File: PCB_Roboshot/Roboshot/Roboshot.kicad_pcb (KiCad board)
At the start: 2 copper layers, 78.3 x 91.9 mm, 28 parts, among them J1 Conn_01x01, J2 Conn_01x08, J3 Conn_01x04, J5 Conn_01x01, Q1_LIGHT1 BC546, Q2_PUMP_DC1 BC546, U1 7840-0000PR

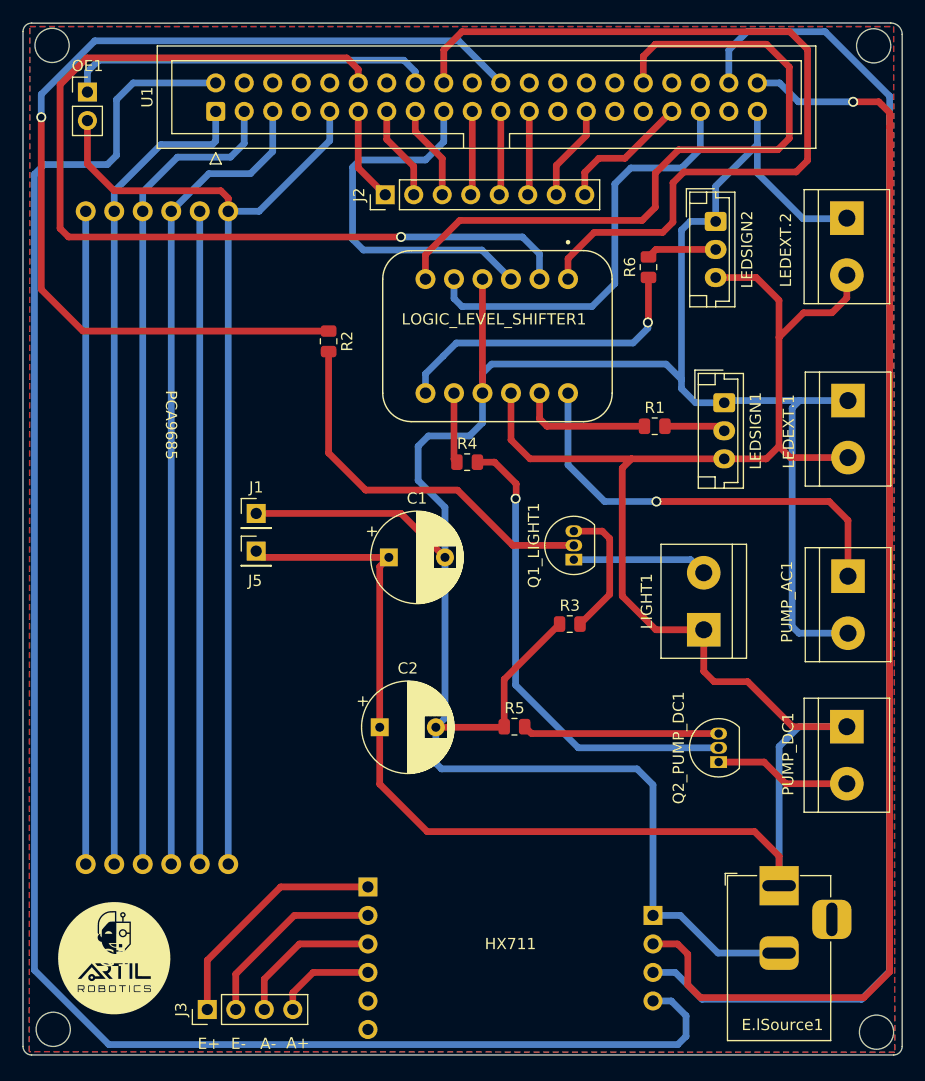
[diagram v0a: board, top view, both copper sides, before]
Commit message: Cambios en PCB roboshot_final
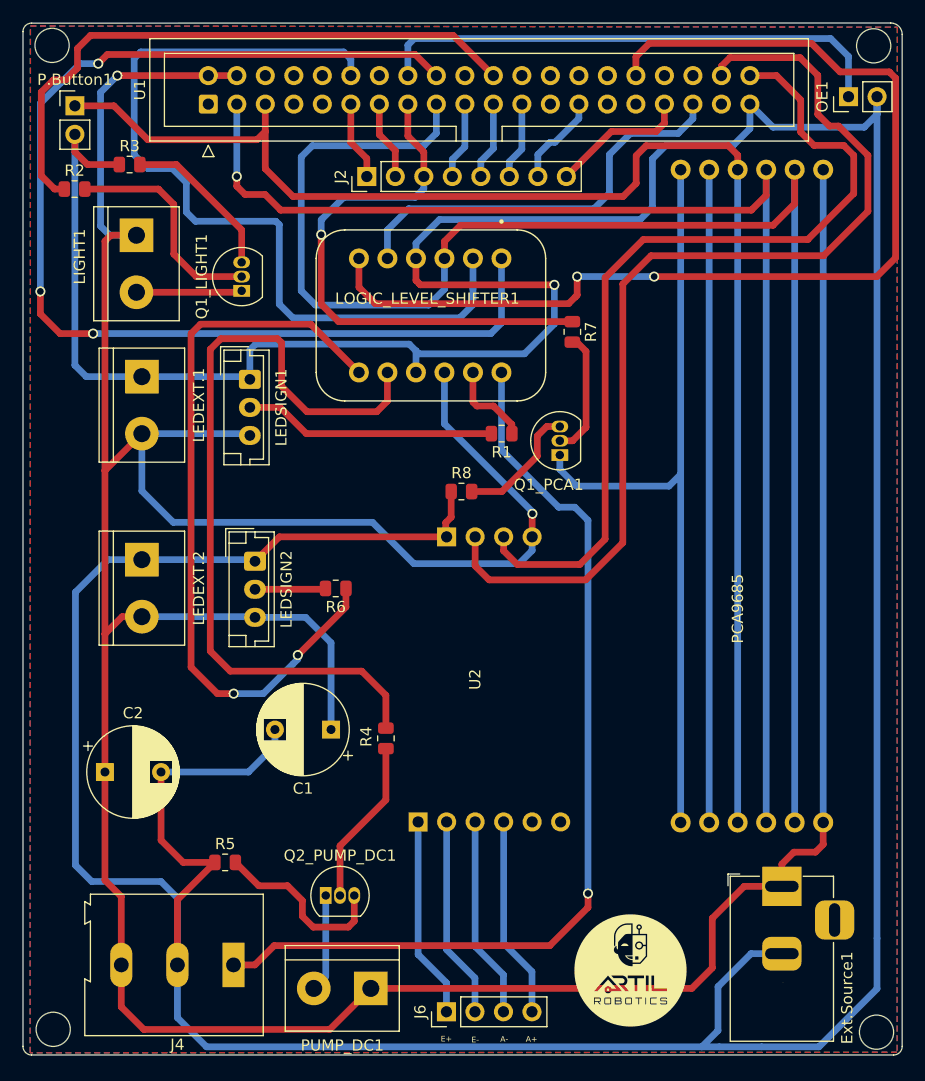
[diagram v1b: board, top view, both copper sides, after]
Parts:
- removed E.lSource1: Conn_01x02, Connector_BarrelJack:BarrelJack_Horizontal
- removed G1: LOGO, Sellos:Sello_completo
- removed HX711: DualChannel, DualChannel_HX711:Dual Channel
- removed J1, J5: Conn_01x01, Connector_PinHeader_2.54mm:PinHeader_1x01_P2.54mm_Vertical
- removed J3: Conn_01x04, Connector_PinHeader_2.54mm:PinHeader_1x04_P2.54mm_Vertical
- removed PUMP_AC1: Conn_01x02, TerminalBlock:TerminalBlock_bornier-2_P5.08mm
- added Ext.Source1: Conn_01x02, Connector_BarrelJack:BarrelJack_Horizontal, F.Cu at (291.9, 185.3)
- added G: LOGO, Sensor:Sello1_artil, F.Cu at (278.4, 192.8)
- added J4: Conn_01x03, TerminalBlock:TerminalBlock_Altech_AK300-3_P5.00mm, F.Cu at (243.0, 192.3)
- added J6: Conn_01x04, Connector_PinHeader_2.54mm:PinHeader_1x04_P2.54mm_Vertical, F.Cu at (262.0, 196.4)
- added P.Button1: Conn_01x02, Connector_PinHeader_2.54mm:PinHeader_1x02_P2.54mm_Vertical, F.Cu at (228.9, 115.7)
- added Q1_PCA1: BC546, Package_TO_SOT_THT:TO-92_Inline, F.Cu at (272.1, 146.8)
- added R7: R, Resistor_SMD:R_0805_2012Metric, F.Cu at (273.2, 135.9)
- added R8: R, Resistor_SMD:R_0805_2012Metric, F.Cu at (263.3, 150.1)
- added U2: H, DualChannel_HX711:Dual Channel, F.Cu at (272.2, 179.5)
- moved LEDEXT.2 69.8 mm to (234.9, 156.2)
- moved OE1 67.8 mm to (297.8, 114.9), turned to 90 degrees
- moved LEDEXT.1 63.0 mm to (234.9, 139.9)
- moved LIGHT1 61.6 mm to (234.4, 127.3), turned to -90 degrees
- moved R3 56.7 mm to (233.8, 121.0)
- moved PCA9685 54.0 mm to (288.5, 160.5), turned to 90 degrees
- moved LEDSIGN2 51.0 mm to (245.0, 156.3)
- moved PUMP_DC1 48.4 mm to (255.3, 194.4), turned to 180 degrees
- moved LEDSIGN1 42.3 mm to (244.5, 140.1)
- moved R6 39.9 mm to (252.1, 158.7), turned to 180 degrees
- moved Q1_LIGHT1 38.1 mm to (243.8, 132.2)
- moved Q2_PUMP_DC1 37.0 mm to (251.3, 186.1), turned to 0 degrees
- moved R5 28.5 mm to (242.3, 183.1)
- moved R2 26.4 mm to (228.9, 123.1), turned to 0 degrees
- moved R4 25.7 mm to (256.6, 172.1), turned to -90 degrees
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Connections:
- C1 pad 1: +5VA -> +5V
- C2 pad 1: +5VA -> +5V
- LEDEXT.1 pad 2: +5VA -> +5V
- LEDEXT.2 pad 2: +5VA -> +5V
- LEDSIGN1 pad 3: +5VA -> +5V
- LEDSIGN2 pad 3: +5VA -> +5V
- LIGHT1 pad 1: +5VA -> +5V
- LOGIC_LEVEL_SHIFTER1 pad HV: +5VA -> +5V
- PCA9685 pad GND_1: GND -> /GND_PCA9685
- PCA9685 pad GND_2: GND -> /GND_PCA9685
- PCA9685 pad V+_1: Net-(PCA9685-PadV+_1) -> +5V
- PCA9685 pad V+_2: Net-(PCA9685-PadV+_1) -> +5V
- PUMP_DC1 pad 1: +5VA -> +5V
- U1 pad 1: +3V3 -> unconnected-(U1-Pad1)
- U1 pad 14: GND -> unconnected-(U1-Pad14)
- U1 pad 20: GND -> unconnected-(U1-Pad20)
- U1 pad 25: GND -> unconnected-(U1-Pad25)
- U1 pad 30: GND -> unconnected-(U1-Pad30)
- U1 pad 34: GND -> unconnected-(U1-Pad34)
- U1 pad 6: GND -> unconnected-(U1-Pad6)
- U1 pad 9: GND -> unconnected-(U1-Pad9)
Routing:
- net +5VA: track 197.0 -> 0.00 mm
- net +5V: track 159.8 -> 340.0 mm, vias 0 -> 2
- net GND: track 322.9 -> 425.7 mm, vias 0 -> 1
- net /GND_PCA9685: track 0.00 -> 71.3 mm
- net /HV3: track 6.26 -> 71.2 mm
- net Net-(PCA9685-PadV+_1): track 58.2 -> 0.00 mm
- net /GPIO3(SCL1): track 73.0 -> 130.5 mm
- net /HV1: track 38.4 -> 85.4 mm
- net /GPIO2(SDA1): track 73.6 -> 116.3 mm, vias 0 -> 1
- net /GPIO22(GEN3): track 8.42 -> 49.0 mm, vias 0 -> 1
- net /HV4: track 27.8 -> 66.6 mm, vias 1 -> 2
- net /GPIO21(SPI1_SCK): track 115.1 -> 77.5 mm, vias 1 -> 0
- net /GPIO25(GEN6): track 89.0 -> 54.9 mm, vias 1 -> 0
- net /GPIO12(PWM0): track 63.7 -> 96.2 mm, vias 0 -> 2
- net +3V3: track 107.3 -> 139.4 mm
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
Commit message: Placa final_Roboshot
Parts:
- removed G: LOGO, Sensor:Sello1_artil
- removed J4: Conn_01x03, TerminalBlock:TerminalBlock_Altech_AK300-3_P5.00mm
- removed P.Button1: Conn_01x02, Connector_PinHeader_2.54mm:PinHeader_1x02_P2.54mm_Vertical
- removed Q1_PCA1, Q2_PUMP_DC1: BC546, Package_TO_SOT_THT:TO-92_Inline
- removed R3: R, Resistor_SMD:R_0805_2012Metric
- removed U2: H, DualChannel_HX711:Dual Channel
- added B.OUTPUT1: BC546, Package_TO_SOT_THT:TO-92_Inline, F.Cu at (239.2, 128.0)
- added BUTTON1: BC546, Package_TO_SOT_THT:TO-92_Inline, F.Cu at (248.7, 183.0)
- added D1: LED, LED_THT:LED_D3.0mm, F.Cu at (228.5, 120.3)
- added HX711: H, DualChannel_HX711:Dual Channel, F.Cu at (268.5, 191.6)
- added IRFZ44N: BSP89, Package_TO_SOT_THT:SIPAK_Vertical, F.Cu at (243.3, 169.1)
- added Q_PCA9685: BC546, Package_TO_SOT_THT:TO-92_Inline, F.Cu at (272.8, 132.9)
- added R10: R, Resistor_SMD:R_0805_2012Metric, F.Cu at (251.8, 188.9)
- added R9: R, Resistor_SMD:R_0805_2012Metric, F.Cu at (231.3, 114.6)
- added ROBOSHOT: ROBOSHOT, Symbol:Sello-ArtilRobotics, F.Cu at (277.8, 193.3)
- added SOLID RELE: Conn_01x03, TerminalBlock:TerminalBlock_Altech_AK300-3_P5.00mm, F.Cu at (234.4, 193.0)
- added SW1: SW_Push_Dual_x2, Connector_PinHeader_2.54mm:PinHeader_1x02_P2.54mm_Vertical, F.Cu at (232.3, 125.9)
- moved R2 71.2 mm to (299.9, 118.1), turned to -90 degrees
- moved OE1 68.0 mm to (231.9, 131.7)
- moved R8 54.5 mm to (227.0, 190.7), turned to -90 degrees
- moved LIGHT1 50.2 mm to (230.7, 177.3)
- moved Q1_LIGHT1 45.5 mm to (242.7, 177.7)
- moved PUMP_DC1 37.7 mm to (230.7, 165.8), turned to -90 degrees
- moved R5 36.0 mm to (238.5, 147.4), turned to 90 degrees
- moved C2 31.8 mm to (256.0, 154.7)
- moved R7 28.8 mm to (299.6, 124.3)
- moved C1 27.1 mm to (271.7, 153.0)
- moved LEDSIGN2 19.6 mm to (243.3, 136.7)
- moved LEDEXT.2 19.1 mm to (230.9, 137.4)
- moved R6 14.7 mm to (252.1, 144.0)
- moved LEDEXT.1 12.8 mm to (230.9, 152.0)
- moved LEDSIGN1 12.3 mm to (243.5, 152.3)
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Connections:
- LIGHT1 pad 1: +5V -> /LIGHT
- LIGHT1 pad 2: /LIGHT -> GND
- LOGIC_LEVEL_SHIFTER1 pad LV1: /GPIO24(GEN5) -> /GPIO12(PWM0)
- LOGIC_LEVEL_SHIFTER1 pad LV2: /GPIO18(GEN1)(PWM0) -> /GPIO19(SPI1_MISO)
- LOGIC_LEVEL_SHIFTER1 pad LV3: /GPIO19(SPI1_MISO) -> /GPIO18(GEN1)(PWM0)
- LOGIC_LEVEL_SHIFTER1 pad LV4: /GPIO12(PWM0) -> /GPIO24(GEN5)
- PCA9685 pad GND_1: /GND_PCA9685 -> GND
- PCA9685 pad GND_2: /GND_PCA9685 -> GND
- PCA9685 pad V+_1: +5V -> /2N_PCA9685
- PCA9685 pad V+_2: +5V -> /2N_PCA9685
- PCA9685 pad VCC_1: +3V3 -> +5V
- PCA9685 pad VCC_2: +3V3 -> +5V
- Q1_LIGHT1 pad 1: /LIGHT -> +5V
- Q1_LIGHT1 pad 3: Net-(Q1_LIGHT1-Pad3) -> /LIGHT
- R1 pad 1: /HV2 -> /HV1
- R4 pad 1: /HV3 -> /HV2
- R4 pad 2: Net-(Q2_PUMP_DC1-Pad2) -> GND
- R5 pad 1: GND -> +5V
- R6 pad 1: /HV4 -> /HV3
- R7 pad 1: /GPIO22(GEN3) -> /GPIO26
- R8 pad 1: GND -> /GPIO14(TXD0)
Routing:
- net +3V3: track 139.4 -> 26.0 mm
- net /GPIO14(TXD0): track 0.00 -> 99.9 mm
- net Net-(Q1_LIGHT1-Pad2): track 19.8 -> 116.4 mm
- net /2N_PCA9685: track 0.00 -> 87.7 mm
- net /HV1: track 85.4 -> 3.57 mm, vias 1 -> 0
- net /GPIO20(SPI1_MOSI): track 90.1 -> 164.7 mm, vias 0 -> 1
- net /GPIO21(SPI1_SCK): track 77.5 -> 149.0 mm, vias 0 -> 1
- net /GND_PCA9685: track 71.3 -> 0.00 mm
- net /HV3: track 71.2 -> 5.01 mm
- net /GPIO24(GEN5): track 104.6 -> 56.8 mm, vias 3 -> 0
- net /HV2: track 7.75 -> 51.3 mm, vias 0 -> 1
- net /GPIO22(GEN3): track 49.0 -> 7.44 mm, vias 1 -> 0
- net /GPIO12(PWM0): track 96.2 -> 62.5 mm, vias 2 -> 0
- net /GPIO18(GEN1)(PWM0): track 76.4 -> 47.3 mm
- net +5V: track 340.0 -> 368.1 mm, vias 2 -> 0
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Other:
- outline, holes or cut-outs redrawn

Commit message: Placa_reducida tamaño
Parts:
- moved Q_PCA9685 16.3 mm to (263.6, 146.4), turned to 0 degrees
- moved R1 8.22 mm to (255.8, 146.8)
- moved R9 7.12 mm to (235.0, 120.7)
- moved R7 6.24 mm to (295.0, 128.4)
- moved C2 6.08 mm to (250.7, 157.7)
- moved C1 4.82 mm to (267.2, 154.4)
- moved PCA9685 4.03 mm to (284.9, 160.1)
- moved J2 3.79 mm to (251.0, 121.2)
- moved R2 3.65 mm to (296.2, 117.7)
- moved R8 1.99 mm to (228.8, 189.7)
- moved HX711 1.25 mm to (268.4, 192.8)
- moved Ext.Source1 0.60 mm to (289.7, 185.3)
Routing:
- net +5V: track 368.1 -> 320.9 mm
- net Net-(Q_PCA9685-Pad2): track 30.3 -> 52.1 mm
- net /2N_PCA9685: track 87.7 -> 104.1 mm
- net Net-(LEDSIGN1-Pad2): track 27.5 -> 15.3 mm
- net /HV1: track 3.57 -> 13.1 mm
- net GND: track 439.7 -> 433.5 mm, vias 2 -> 1
- net /GPIO3(SCL1): track 129.2 -> 123.8 mm
- net +3V3: track 26.0 -> 31.3 mm
- net /GPIO12(PWM0): track 62.5 -> 57.2 mm
- net /GPIO21(SPI1_SCK): track 149.0 -> 144.2 mm
- net /GPIO14(TXD0): track 99.9 -> 103.6 mm
- net /GPIO20(SPI1_MOSI): track 164.7 -> 161.2 mm
- net /GPIO2(SDA1): track 120.2 -> 116.8 mm
- net Net-(Q1_LIGHT1-Pad2): track 116.4 -> 113.6 mm
- net /GPIO13(PWM1): track 12.4 -> 14.6 mm
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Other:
- board size 78.3 x 91.9 mm -> 73 x 91.9 mm

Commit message: revision de PCB
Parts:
- SCR1: renamed from SOLID RELE
- moved R1 204.6 mm to (92.2, 132.3), turned to 180 degrees
- moved C1 171.8 mm to (95.4, 159.6), turned to 90 degrees
- moved R9 171.6 mm to (92.2, 125.9), turned to 0 degrees
- moved R3 171.6 mm to (123.7, 118.8), turned to 180 degrees
- moved BUTTON1 171.3 mm to (88.0, 123.5), turned to 90 degrees
- moved Ext.Source1 166.7 mm to (123.0, 181.7), turned to 180 degrees
- moved LOGIC_LEVEL_SHIFTER1 166.3 mm to (104.7, 125.6)
- moved PCA1 162.6 mm to (124.6, 133.3), turned to -90 degrees
- moved ROBOSHOT 162.6 mm to (115.8, 179.6)
- moved Q1_LIGHT1 160.5 mm to (88.0, 134.7)
- moved U1 156.4 mm to (83.4, 108.3)
- moved IRFZ44N1 156.0 mm to (87.4, 165.2), turned to -90 degrees
- moved LIGHT1 155.9 mm to (81.1, 133.4)
- moved U2 155.7 mm to (113.9, 172.7)
- moved LoadCell1 155.7 mm to (101.2, 179.1)
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- renumbered IRFZ44N to IRFZ44N1, J2 to J1, J6 to LoadCell1, PCA9685 to PCA1, Q_PCA9685 to Q_PCA1, R2 to R1, R4 to R2, R7 to R3, R1 to R4, R6 to R5, R5 to R6, R8 to R7, R9 to R8, R10 to R9, HX711 to U2
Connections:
- LIGHT1 pad 1: /LIGHT -> GND
- LIGHT1 pad 2: GND -> /LIGHT
- LOGIC_LEVEL_SHIFTER1 pad HV1: /HV1 -> /HV4
- LOGIC_LEVEL_SHIFTER1 pad HV3: /HV3 -> /HV1
- LOGIC_LEVEL_SHIFTER1 pad HV4: /HV4 -> /HV3
- PUMP_DC1 pad 1: +5V -> /PUMP
- PUMP_DC1 pad 2: /PUMP -> +5V
- U1 pad 1: unconnected-(U1-Pad1) -> +3V3
- U1 pad 14: unconnected-(U1-Pad14) -> GND
- U1 pad 20: unconnected-(U1-Pad20) -> GND
- U1 pad 25: unconnected-(U1-Pad25) -> GND
- U1 pad 30: unconnected-(U1-Pad30) -> GND
- U1 pad 34: unconnected-(U1-Pad34) -> GND
- U1 pad 6: unconnected-(U1-Pad6) -> GND
- U1 pad 9: unconnected-(U1-Pad9) -> GND
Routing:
- net Net-(Q1_LIGHT1-Pad2): track 113.6 -> 3.75 mm
- net /2N_PCA9685: track 104.1 -> 3.86 mm
- net /GPIO20(SPI1_MOSI): track 161.2 -> 72.3 mm, vias 1 -> 0
- net /GPIO21(SPI1_SCK): track 144.2 -> 61.7 mm, vias 1 -> 0
- net /GPIO2(SDA1): track 116.8 -> 40.4 mm
- net /GPIO14(TXD0): track 103.6 -> 37.1 mm
- net +5V: track 320.9 -> 257.5 mm
- net GND: track 433.5 -> 373.5 mm, vias 1 -> 0
- net Net-(PCA1-PadOE_1): track 58.2 -> 0.00 mm
- net Net-(Q_PCA1-Pad2): track 52.1 -> 5.31 mm
- net /GPIO25(GEN6): track 41.8 -> 88.6 mm
- net /GPIO3(SCL1): track 123.8 -> 98.8 mm, vias 1 -> 0
- net /GPIO23(GEN4): track 55.8 -> 35.0 mm, vias 1 -> 0
- net Net-(BUTTON1-Pad2): track 23.7 -> 3.29 mm
- net Net-(B.OUTPUT1-Pad2): track 19.6 -> 3.45 mm
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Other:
- board size 73 x 91.9 mm -> 62.8 x 85.9 mm
